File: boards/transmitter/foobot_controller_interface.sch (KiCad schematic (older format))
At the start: 23 parts, among them IC1 ATTINY13A-SS, K2 TX, P10 AUX_IN, P11 AUX, P12 AUX, P15 ¬Q7, P2 SMS, P3 NES, P35 CHANNEL_X, P36 CONN_1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

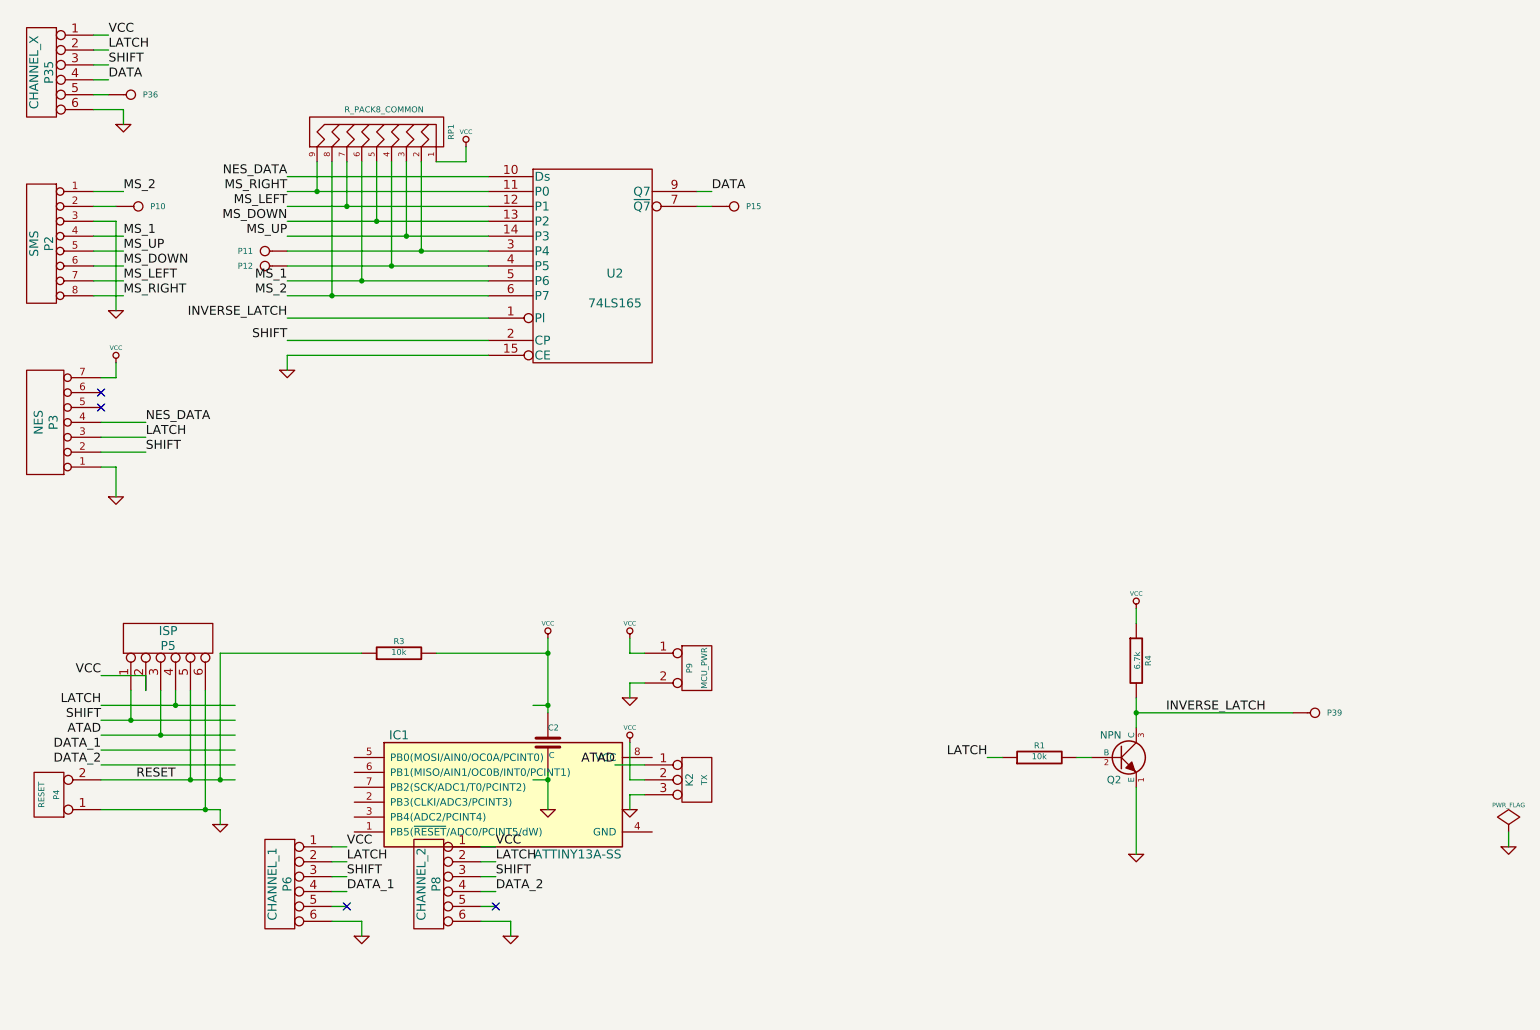
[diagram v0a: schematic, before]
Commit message: Fix microcontroller location in foobot_controller_interface.sch Plot schematics for the circuits.
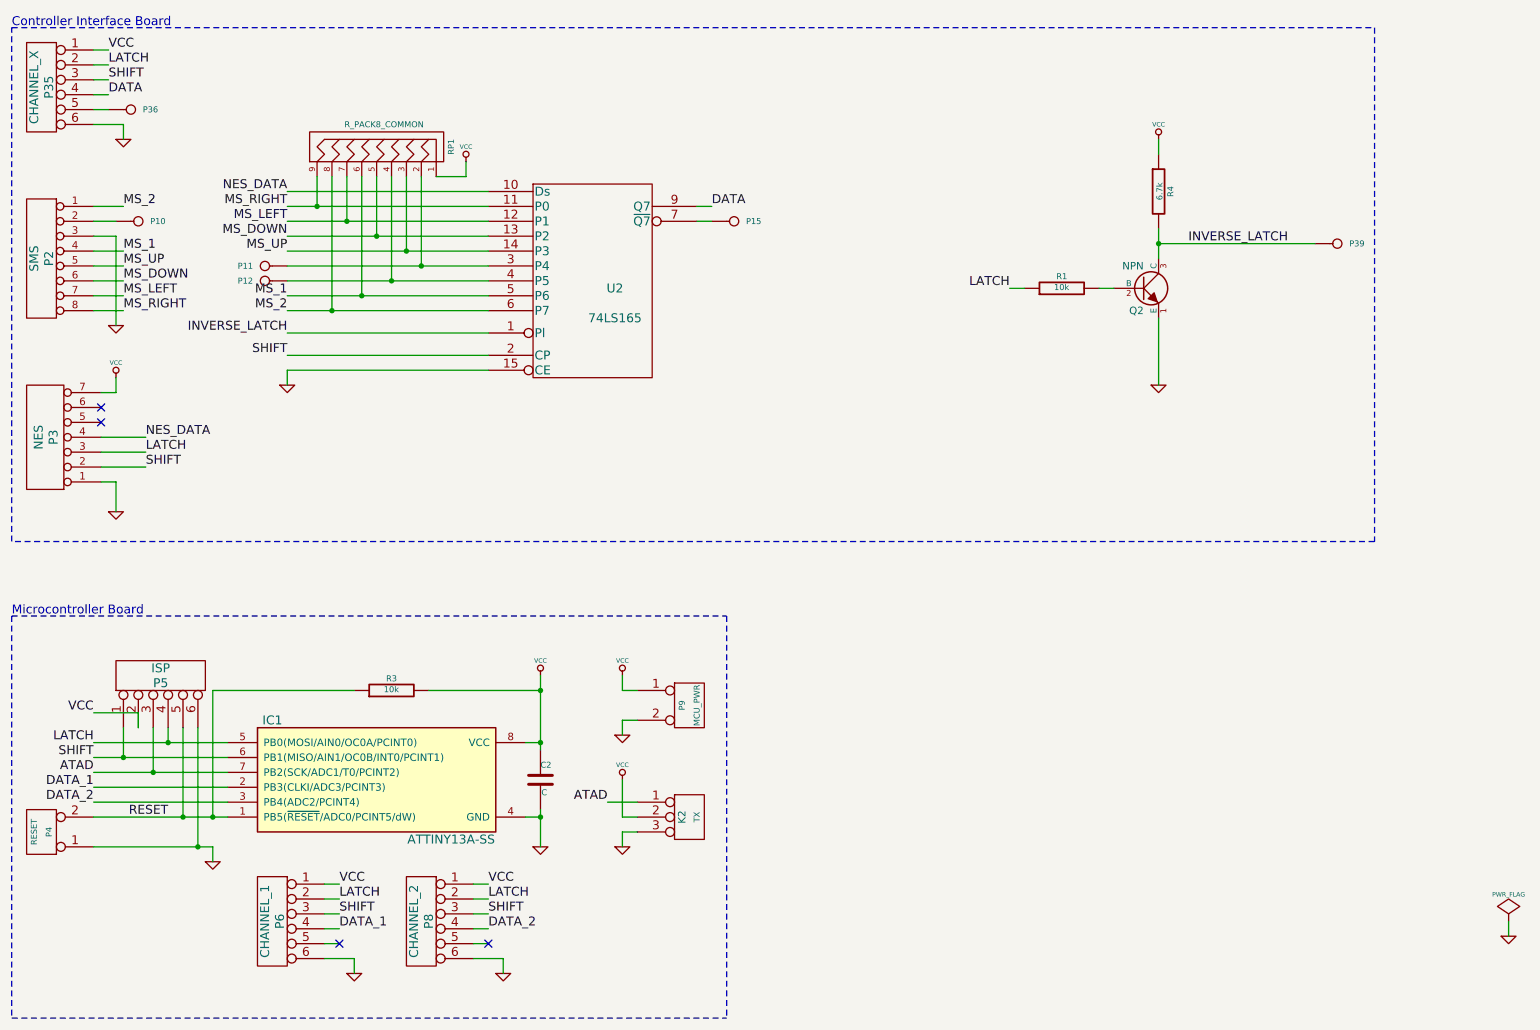
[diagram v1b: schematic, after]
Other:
- note added: "Controller Interface Board"
- note added: "Microcontroller Board"
- moved on the sheet: C2, IC1, K2, P10, P11, P12, P15, P2, P3, P35, P36, P39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
